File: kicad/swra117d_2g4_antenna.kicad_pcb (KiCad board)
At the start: 2 copper layers, 40 x 30 mm, 2 parts, among them J1 SMA edge launch

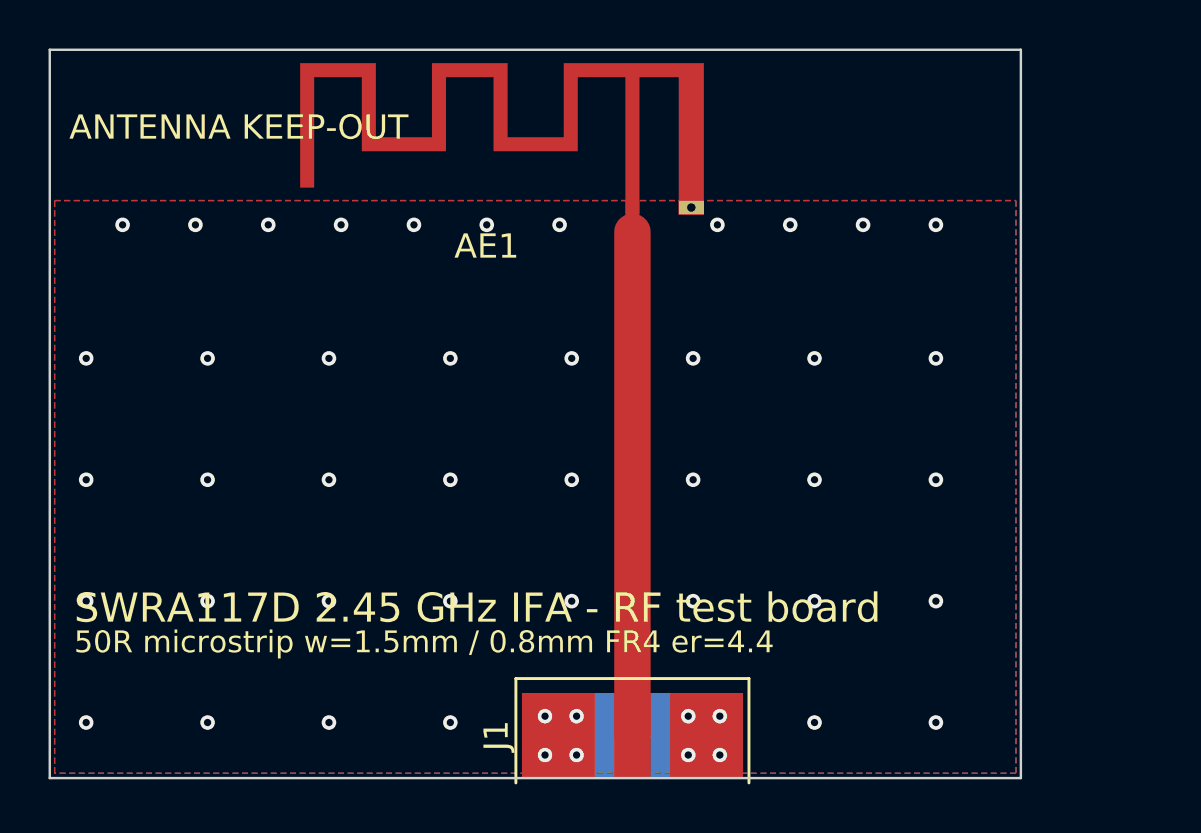
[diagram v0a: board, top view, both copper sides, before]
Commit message: Revert the x1.155 retune: the 2.83 GHz result came from an invalid setup
The RFsim layout plot shows the only copper in the model is the antenna, the
feed line and the connector pads - the ground pours were unfilled, so the
antenna had no ground plane. An inverted-F radiates against its plane; the
plane is half the antenna, and the 49 stitching vias connected to nothing.
The same dialog was set to RFsim's FR-4 preset, 1.6 mm / er 4.5, not this
board's 0.8 mm / er 4.4: its own 50 ohm port width guess of 3.114 mm is the
50 ohm width for 1.6 mm / er 4.5, where ours is 1.49 mm (and our 1.5 mm line
would be 71 ohm on 1.6 mm). Two large errors pulling opposite ways, so the
2.83 GHz cannot be used - and a 15% geometry change justified by it should
not stand.

ANT_SCALE is back to 1.0 on the published footprint. The scaled copy and
scale_footprint.py stay, as the retune path for when a valid run exists.

check_project.py caught its own bug while reverting: it held the ground
plane edge as a hardcoded 65.75, so once the antenna moved it reported the
board as broken. It now reads the edge from the board's copper zones, which
is where gen_project.py derives it from in the first place.

README now leads with the four settings that decide whether a run of this
board means anything: fill the zones, substrate 0.8 mm / er 4.4, domain
margin >= 31 mm (lambda/4 at 2.45 GHz, not the 4 mm default, which puts the
absorbing boundary lambda/31 from the antenna), and a port attached to the
feed line as CPW rather than Lumped with "No Line". Also a section
separating the three edges that are easy to conflate: the board edge (do not
extend it past the antenna - dielectric beside the arm loads it and pulls
resonance down), the ground plane keep-out edge (never extend copper into
it), and the simulation domain edge (this is the one to extend).

Co-Authored-By: Claude Opus 5 <noreply@anthropic.com>
Claude-Session: https://claude.ai/code/session_01Prj6bUQ2KQzzxzD4bgtswJ
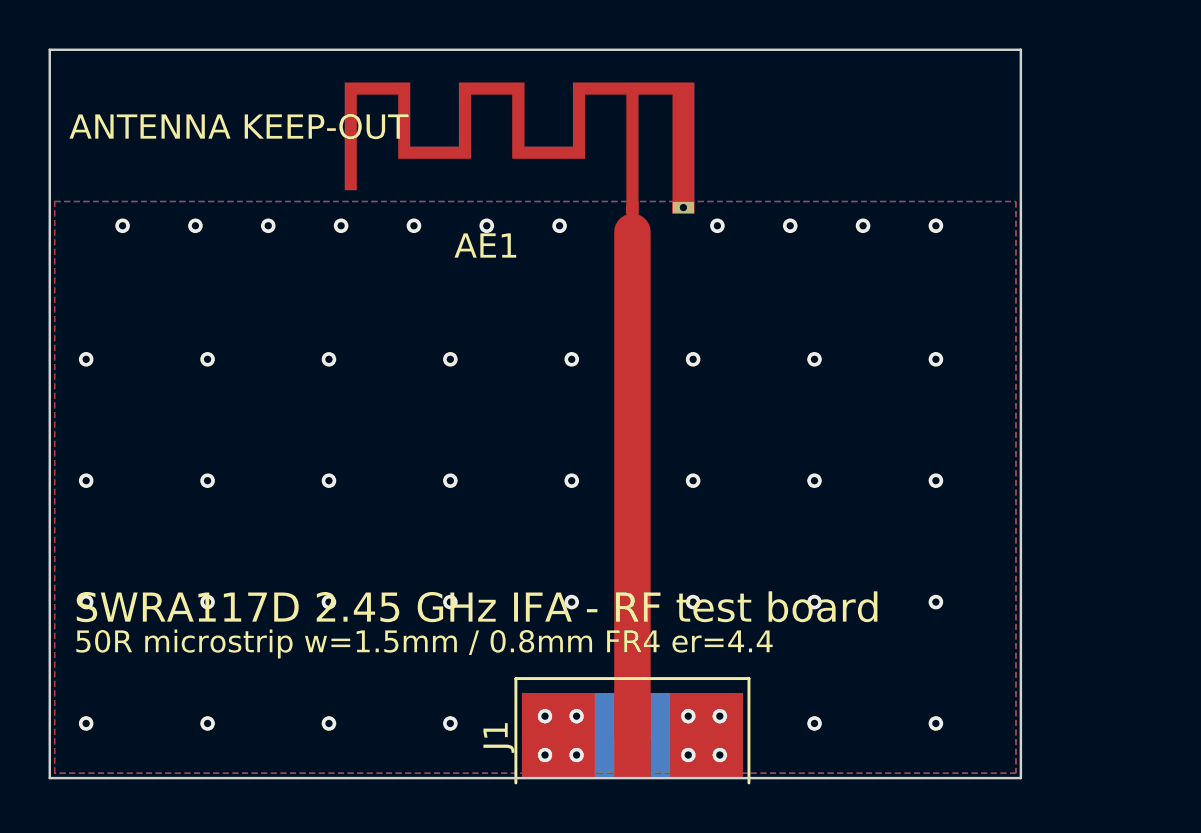
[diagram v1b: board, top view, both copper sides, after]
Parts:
- AE1: footprint SWRA117D_RF:SWRA117D_2G4_Left_retuned -> SWRA117D_RF:Texas_SWRA117D_2.4GHz_Left

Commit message: Rebuild the board for 1.6 mm FR4: the board owner says that is the stackup
The simulator was right and this project's assumption was wrong. The 0.8 mm
FR4 was picked here for a convenient line width and never verified; the
fabricated board is 1.6 mm, so the design follows the board. Stackup is now
1.6 mm / er 4.5 to match what RFsim runs.

Everything downstream is derived, so it was one constant plus a new
generator:

- 50 ohm microstrip 1.50 -> 2.95 mm (50.2 ohm)
- tools/gen_sma_footprint.py generates the connector for the stackup: signal
  pad 2.95 mm, coplanar gap 2.0 mm (launch 49.8 ohm, where the old 0.8 mm gap
  would give 45.1 ohm on this substrate), bottom ground pad 12.95 mm across
- top pour keep-away 1.0 -> 2.0 mm, and the stitching vias follow the
  connector's new pad centres

Two geometric consequences needed deciding rather than deriving. A 2.95 mm
line cannot butt against the antenna's 0.5 mm feed pad - the step would be a
real discontinuity and the wide line would crowd the antenna's ground pin at
0.175 mm - so the last 4.5 mm tapers to 0.5 mm in six stages. And the pour
corridor now starts 3 mm below the plane edge: at 2.0 mm either side it would
otherwise cut a 7 mm notch into the ground plane edge directly under the
antenna, and that edge is part of the antenna.

The antenna itself is untouched and still matches SWRA117D Table 1 exactly.
Stitching is 41 vias with a worst unstitched span of 9.1 mm (7.8 GHz).

The feed-width guard earned itself: the first attempt at this edit failed
partway, leaving a 1.5 mm line against the new 2.95 mm port pad, and the
check caught exactly that.

Co-Authored-By: Claude Opus 5 <noreply@anthropic.com>
Claude-Session: https://claude.ai/code/session_01Prj6bUQ2KQzzxzD4bgtswJ
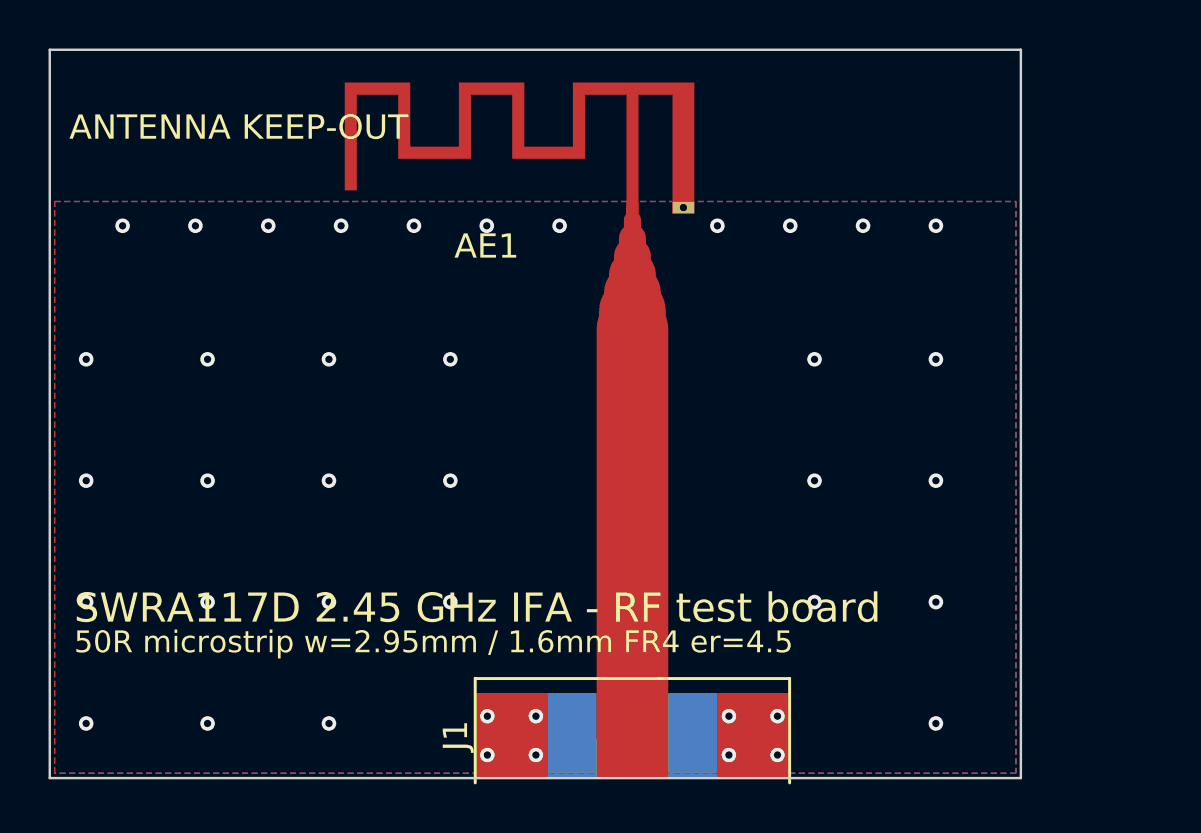
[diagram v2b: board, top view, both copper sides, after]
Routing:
- net GND: vias 49 -> 41
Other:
- board text added: "50R microstrip w=2.95mm / 1.6mm FR4 er=4.5"
- board text removed: "50R microstrip w=1.5mm / 0.8mm FR4 er=4.4"
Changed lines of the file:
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@@
 	(generator "gen_project.py")
 	(generator_version "9.0")
-	(general (thickness 0.89) (legacy_teardrops no))
+	(general (thickness 1.69) (legacy_teardrops no))
 	(paper "A4")
 	(title_block
@@
 		(date "2026-09-12")
 		(rev "A")
-		(comment 1 "2 layer, 0.8 mm FR4, 35 um Cu")
-		(comment 2 "50 ohm microstrip w = 1.5 mm, no matching network")
+		(comment 1 "2 layer, 1.6 mm FR4, 35 um Cu")
+		(comment 2 "50 ohm microstrip w = 2.95 mm, no matching network")
 	)
 	(layers
@@
 				(type "core")
 				(material "FR4")
-				(thickness 0.8)
-				(epsilon_r 4.4)
+				(thickness 1.6)
+				(epsilon_r 4.5)
 				(loss_tangent 0.02)
 			)
@@
 		(layer "F.Cu")
 		(at 124 90 90)
-		(descr "Generic end-launch (edge-mount) SMA jack for a 0.8 mm two layer board. Origin sits on the board edge: the signal pad starts at x = 0 and the connector body hangs off the outside of the Edge.Cuts line. Pad 1 = signal, pad 2 = shell ground: two tabs either side of the signal pad on the top, one solid plane under the whole launch on the bottom, so the launch keeps its reference without relying on a zone fill."
+		(descr "Generic end-launch (edge-mount) SMA jack, generated for a 1.6 mm substrate (er 4.5). Signal pad 2.95 mm wide to match the 50 ohm line; coplanar ground set back 2.0 mm, which makes the launch 49.8 ohm. Origin sits on the board edge. Pad 1 = signal, pad 2 = shell ground: two tabs on top, one solid plane underneath so the launch keeps its reference without relying on a zone fill."
 		)
 		(tags "SMA edge launch end launch RF connector 50 ohm")
 		(attr smd)
 		(property "Reference" "J1"
-			(at 1.75 -5.6 90)
+			(at 1.75 -7.275 90)
 			(layer "F.SilkS")
 			(effects (font (size 1 1) (thickness 0.15)))
@@
 		)
 		(property "Value" "SMA edge launch"
-			(at 1.75 5.6 90)
+			(at 1.75 7.275 90)
 			(layer "F.Fab")
 			(effects (font (size 1 1) (thickness 0.15)))
@@
 		)
 		(fp_line
-			(start -0.2 -4.8)
-			(end 4.1 -4.8)
+			(start -0.2 -6.475)
+			(end 4.1 -6.475)
 			(stroke (width 0.12) (type solid))
 			(layer "F.SilkS")
 		)
 		(fp_line
-			(start -0.2 4.8)
-			(end 4.1 4.8)
+			(start -0.2 6.475)
+			(end 4.1 6.475)
 			(stroke (width 0.12) (type solid))
 			(layer "F.SilkS")
 		)
 		(fp_line
-			(start 4.1 -4.8)
-			(end 4.1 4.8)
+			(start 4.1 -6.475)
+			(end 4.1 6.475)
 			(stroke (width 0.12) (type solid))
 			(layer "F.SilkS")
 		)
 		(fp_line
-			(start -0.2 -4.8)
-			(end 4.1 -4.8)
+			(start -0.2 -6.475)
+			(end 4.1 -6.475)
 			(stroke (width 0.1) (type solid))
 			(layer "F.Fab")
 		)
 		(fp_line
-			(start -0.2 4.8)
-			(end 4.1 4.8)
+			(start -0.2 6.475)
+			(end 4.1 6.475)
 			(stroke (width 0.1) (type solid))
 			(layer "F.Fab")
 		)
 		(fp_line
-			(start 4.1 -4.8)
-			(end 4.1 4.8)
+			(start 4.1 -6.475)
+			(end 4.1 6.475)
 			(stroke (width 0.1) (type solid))
 			(layer "F.Fab")
 		)
-		(fp_line
-			(start -0.2 -4.8)
-			(end -0.2 4.8)
-			(stroke (width 0.1) (type solid))
-			(layer "F.Fab")
-		)
 		(fp_rect
-			(start -0.4 -5.0)
-			(end 4.3 5.0)
+			(start -0.4 -6.675)
+			(end 4.3 6.675)
 			(stroke (width 0.05) (type solid))
 			(fill no)
@@
 		)
 		(fp_rect
-			(start -0.4 -5.0)
-			(end 4.3 5.0)
+			(start -0.4 -6.675)
+			(end 4.3 6.675)
 			(stroke (width 0.05) (type solid))
 			(fill no)
@@
 		(pad "1" smd rect
 			(at 1.75 0 90)
-			(size 3.5 1.5)
+			(size 3.5 2.95)
 			(layers "F.Cu" "F.Paste" "F.Mask")
 			(net 2 "ANT_FEED")
@@
 		)
 		(pad "2" smd rect
-			(at 1.75 -3.05 90)
+			(at 1.75 -4.975 90)
 			(size 3.5 3)
 			(layers "F.Cu" "F.Paste" "F.Mask")
@@
 		)
 		(pad "2" smd rect
-			(at 1.75 3.05 90)
+			(at 1.75 4.975 90)
 			(size 3.5 3)
 			(layers "F.Cu" "F.Paste" "F.Mask")
@@
 		(pad "2" smd rect
 			(at 1.75 0 90)
-			(size 3.5 9.1)
+			(size 3.5 12.95)
 			(layers "B.Cu" "B.Paste" "B.Mask")
 			(net 1 "GND")
@@
 		(effects (font (size 1.2 1.2) (thickness 0.15)) (justify left))
 	)
-	(gr_text "50R microstrip w=1.5mm / 0.8mm FR4 er=4.4"
+	(gr_text "50R microstrip w=2.95mm / 1.6mm FR4 er=4.5"
 		(at 101 84.4 0)
 		(layer "F.SilkS")
@@
 	(segment
 		(start 124 88.25)
-		(end 124 67.5)
-		(width 1.5)
+		(end 124 71.5)
+		(width 2.95)
 		(layer "F.Cu")
 		(net 2)
 	)
 	(segment
-		(start 124 67.5)
+		(start 124 71.5)
+		(end 124 70.75)
+		(width 2.746)
+		(layer "F.Cu")
+		(net 2)
+	)
+	(segment
+		(start 124 70.75)
+		(end 124 70)
+		(width 2.338)
+		(layer "F.Cu")
+		(net 2)
+	)
+	(segment
+		(start 124 70)
+		(end 124 69.25)
+		(width 1.929)
+		(layer "F.Cu")
+		(net 2)
+	)
+	(segment
+		(start 124 69.25)
+		(end 124 68.5)
+		(width 1.521)
+		(layer "F.Cu")
+		(net 2)
+	)
+	(segment
+		(start 124 68.5)
+		(end 124 67.75)
+		(width 1.113)
+		(layer "F.Cu")
+		(net 2)
+	)
+	(segment
+		(start 124 67.75)
+		(end 124 67)
+		(width 0.704)
+		(layer "F.Cu")
+		(net 2)
+	)
+	(segment
+		(start 124 67)
 		(end 124 66.5)
 		(width 0.5)
@@
 	)
 	(via
-		(at 120.4 87.45)
-		(size 0.6)
-		(drill 0.3)
-		(layers "F.Cu" "B.Cu")
-		(net 1)
-	)
-	(via
-		(at 120.4 89.05)
-		(size 0.6)
-		(drill 0.3)
-		(layers "F.Cu" "B.Cu")
-		(net 1)
-	)
-	(via
-		(at 121.7 87.45)
-		(size 0.6)
-		(drill 0.3)
-		(layers "F.Cu" "B.Cu")
-		(net 1)
-	)
-	(via
-		(at 121.7 89.05)
-		(size 0.6)
-		(drill 0.3)
-		(layers "F.Cu" "B.Cu")
-		(net 1)
-	)
-	(via
-		(at 126.3 87.45)
-		(size 0.6)
-		(drill 0.3)
-		(layers "F.Cu" "B.Cu")
-		(net 1)
-	)
-	(via
-		(at 126.3 89.05)
-		(size 0.6)
-		(drill 0.3)
-		(layers "F.Cu" "B.Cu")
-		(net 1)
-	)
-	(via
-		(at 127.6 87.45)
-		(size 0.6)
-		(drill 0.3)
-		(layers "F.Cu" "B.Cu")
-		(net 1)
-	)
-	(via
-		(at 127.6 89.05)
+		(at 120.025 87.45)
+		(size 0.6)
+		(drill 0.3)
+		(layers "F.Cu" "B.Cu")
+		(net 1)
+	)
+	(via
+		(at 120.025 89.05)
+		(size 0.6)
+		(drill 0.3)
+		(layers "F.Cu" "B.Cu")
+		(net 1)
+	)
+	(via
+		(at 118.025 87.45)
+		(size 0.6)
+		(drill 0.3)
+		(layers "F.Cu" "B.Cu")
+		(net 1)
+	)
+	(via
+		(at 118.025 89.05)
+		(size 0.6)
+		(drill 0.3)
+		(layers "F.Cu" "B.Cu")
+		(net 1)
+	)
+	(via
+		(at 127.975 87.45)
+		(size 0.6)
+		(drill 0.3)
+		(layers "F.Cu" "B.Cu")
+		(net 1)
+	)
+	(via
+		(at 127.975 89.05)
+		(size 0.6)
+		(drill 0.3)
+		(layers "F.Cu" "B.Cu")
+		(net 1)
+	)
+	(via
+		(at 129.975 87.45)
+		(size 0.6)
+		(drill 0.3)
+		(layers "F.Cu" "B.Cu")
+		(net 1)
+	)
+	(via
+		(at 129.975 89.05)
 		(size 0.6)
 		(drill 0.3)
@@
 	)
 	(via
-		(at 121.5 72.75)
-		(size 0.6)
-		(drill 0.3)
-		(layers "F.Cu" "B.Cu")
-		(net 1)
-	)
-	(via
-		(at 126.5 72.75)
-		(size 0.6)
-		(drill 0.3)
-		(layers "F.Cu" "B.Cu")
-		(net 1)
-	)
-	(via
 		(at 131.5 72.75)
 		(size 0.6)
@@
 	)
 	(via
-		(at 121.5 77.75)
-		(size 0.6)
-		(drill 0.3)
-		(layers "F.Cu" "B.Cu")
-		(net 1)
-	)
-	(via
-		(at 126.5 77.75)
-		(size 0.6)
-		(drill 0.3)
-		(layers "F.Cu" "B.Cu")
-		(net 1)
-	)
-	(via
 		(at 131.5 77.75)
 		(size 0.6)
@@
 	)
 	(via
-		(at 121.5 82.75)
-		(size 0.6)
-		(drill 0.3)
-		(layers "F.Cu" "B.Cu")
-		(net 1)
-	)
-	(via
-		(at 126.5 82.75)
-		(size 0.6)
-		(drill 0.3)
-		(layers "F.Cu" "B.Cu")
-		(net 1)
-	)
-	(via
 		(at 131.5 82.75)
 		(size 0.6)
@@
 	(via
 		(at 111.5 87.75)
-		(size 0.6)
-		(drill 0.3)
-		(layers "F.Cu" "B.Cu")
-		(net 1)
-	)
-	(via
-		(at 116.5 87.75)
-		(size 0.6)
-		(drill 0.3)
-		(layers "F.Cu" "B.Cu")
-		(net 1)
-	)
-	(via
-		(at 131.5 87.75)
 		(size 0.6)
 		(drill 0.3)
@@
 		)
 		(fill (thermal_gap 0.4) (thermal_bridge_width 0.4))
-		(polygon (pts (xy 122.25 66.25) (xy 125.75 66.25) (xy 125.75 90.5) (xy 122.25 90.5)))
+		(polygon (pts (xy 120.525 69.25) (xy 127.475 69.25) (xy 127.475 90.5) (xy 120.525 90.5)))
 	)
 	(embedded_fonts no)
